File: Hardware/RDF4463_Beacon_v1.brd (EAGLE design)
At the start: 100 x 80 mm, 21 parts, among them IC1 LD117AS33TR, M1 DORJI_DRF4463F, U1 PIC18F24K22

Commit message: PCB yi cizmeye basladim
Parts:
- ANT1: value (none) -> ANT
- C1, C2: value (none) -> 15p
- C3: value (none) -> 10n
- LED1: value (none) -> Y
- LED2: value (none) -> K
- Q1: value (none) -> 20M
- R1, R4: value (none) -> 10K
- R2, R3, R5: value (none) -> 1K
- SV1: value (none) -> ICD
- VIN: value (none) -> INPUT
- moved R3 81.1 mm to (-47.0, 44.5), turned to 0 degrees
- moved C4 76.8 mm to (-39.4, 26.7)
- moved LED2 74.5 mm to (-43.2, 50.8), turned to 0 degrees
- moved R2 73.9 mm to (-41.9, 44.5), turned to 0 degrees
- moved C5 71.0 mm to (-27.9, 26.7)
- moved C18 70.5 mm to (-17.8, 38.1), turned to 0 degrees
- moved LED1 68.2 mm to (-36.8, 50.8), turned to 0 degrees
- moved R1 50.7 mm to (-36.8, 44.5), turned to 0 degrees
- moved M1 46.2 mm to (31.8, 45.7)
- moved R5 44.2 mm to (-15.2, 50.8)
- moved C17 43.1 mm to (-48.3, 26.7)
- moved C1 28.4 mm to (19.4, 37.9), turned to 270 degrees
- moved U1 27.6 mm to (32.2, 42.8)
- moved IC1 24.7 mm to (31.8, 53.9)
- moved C2 22.8 mm to (19.4, 45.6), turned to 90 degrees
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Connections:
- removed net GPIO0: M1.3
- removed net GPIO1: M1.4
- removed net N$10: R2.1, R3.1
- removed net N$5: R1.1
- net +3V3: now also M1.6; no longer M1.5
- net GND: now also R2.1, R3.1
- net MCLR: now also R1.1
- net RB6: now also U1.27
- net SCLK: now also U1.24
- net SDI: now also M1.5; no longer M1.7
- net SDO: now also M1.7; no longer M1.6
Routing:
- net GND: track 0.00 -> 23.4 mm
- net N$3: track 0.00 -> 13.6 mm
- net N$4: track 0.00 -> 13.1 mm
- net RB7: track 0.00 -> 8.21 mm
- net RB6: track 0.00 -> 8.11 mm
- net SDN: track 7.13 -> 0.00 mm
- net SDI: track 5.24 -> 0.00 mm
- net SCLK: track 0.00 -> 4.35 mm
- net VCC: track 0.00 -> 3.97 mm
- net N$2: track 0.00 -> 2.17 mm
- net NSEL: track 6.49 -> 4.61 mm
- net NIRQ: track 6.73 -> 4.87 mm
- net SDO: track 5.65 -> 4.23 mm

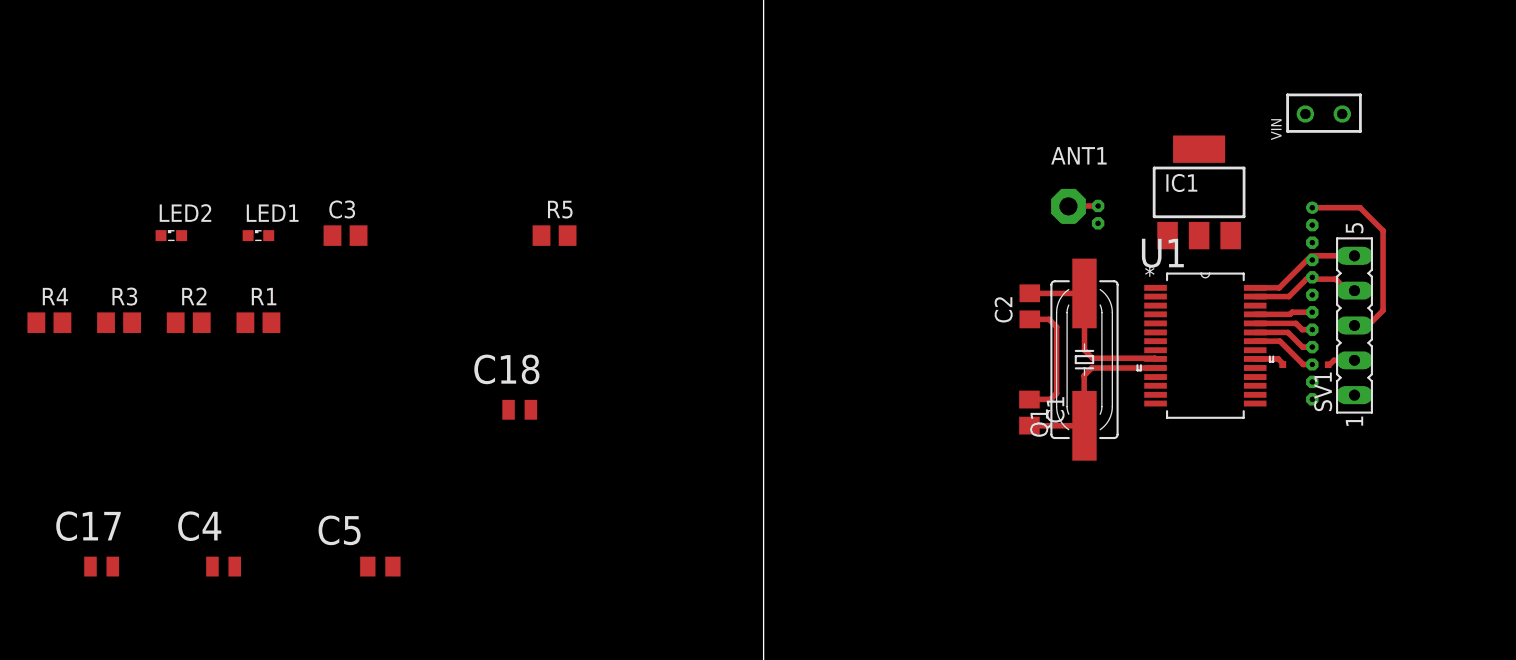
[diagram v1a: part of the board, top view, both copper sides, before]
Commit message: once -SS kilif a gore cizmistim
Bu versiyonda degistiriyorum.. -SO klifli PIC e gorre yaptim

bu kartin buyuk bir bolumunu ICD konnektoru ve DATA RXTX konnektoru tutuyor
simdilik bunu bir EVALUATION karti gibi kullanacagim

Daha sonra yapacaklarim sunlardir :
------------------------------------

1) PIC'i APRS kullanimi icin 16F628 gibi kucuk bir PIC ile degistirmek
2) secilecek PIC'in 3.3V ile calisan versiyonunu tercih etmek
3) MTK GPS i de ekleyip ondan gelen datalari okumak
4) MTK GPS i iceren bir kart cizmek
5) vesaire vesaire
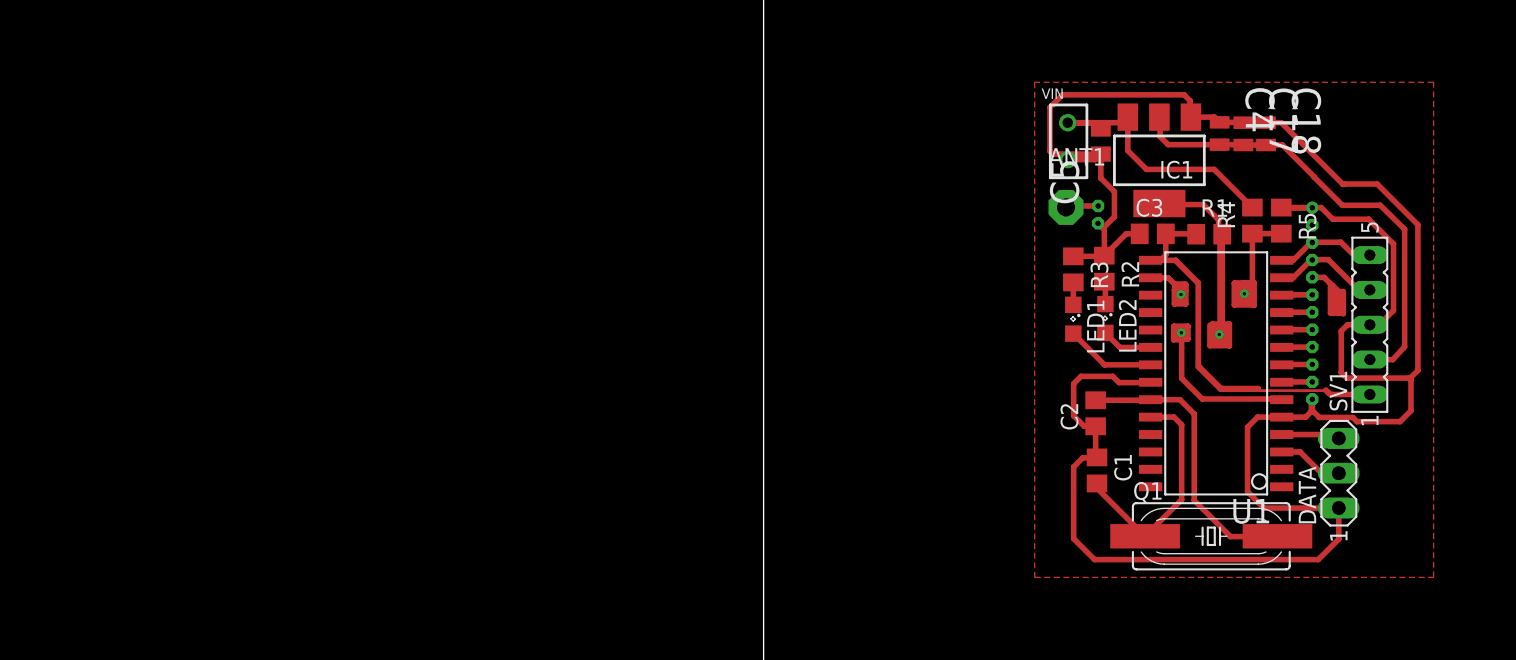
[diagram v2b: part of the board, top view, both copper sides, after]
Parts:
- added DATA: RTX, con-lstb:MA03-1
- LED1, LED2: device led:SML0603 -> led:SML0805
- R5: value 1K -> 1K8
- moved C17 89.0 mm to (35.0, 58.2), turned to 270 degrees
- moved R4 88.0 mm to (35.6, 51.9), turned to 90 degrees
- moved C4 79.2 mm to (33.2, 58.2), turned to 270 degrees
- moved R3 69.7 mm to (22.6, 48.3), turned to 270 degrees
- moved R1 69.6 mm to (32.5, 50.9)
- moved LED2 68.4 mm to (24.9, 44.8), turned to 270 degrees
- moved R2 66.9 mm to (24.8, 48.4), turned to 270 degrees
- moved C5 61.0 mm to (24.6, 57.7), turned to 90 degrees
- moved LED1 59.7 mm to (22.6, 44.7), turned to 270 degrees
- moved C3 58.9 mm to (28.4, 50.9)
- moved C18 58.0 mm to (36.6, 58.2), turned to 270 degrees
- moved R5 53.0 mm to (37.7, 51.9), turned to 270 degrees
- moved VIN 18.1 mm to (22.2, 58.3), turned to 270 degrees
- moved Q1 15.9 mm to (32.6, 28.9), turned to 0 degrees
- moved C2 9.16 mm to (24.2, 37.8)
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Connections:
- removed net +3V3: C17.2, C18.2, C4.2, IC1.4, M1.6
- new net RX: DATA.3, U1.18
- new net TX: DATA.2, U1.17
- net GND: now also DATA.1
- net MCLR: now also C3.2
- net SDI: now also M1.7, U1.25; no longer M1.5, U1.26
- net SDO: now also M1.6, U1.26; no longer M1.7, U1.25
- net VCC: now also C17.2, C18.2, C4.2, IC1.4, M1.5; no longer C3.2
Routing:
- net GND: track 23.4 -> 167.7 mm
- net VCC: track 3.97 -> 67.0 mm
- net MCLR: track 0.00 -> 43.0 mm
- net ADC: track 0.00 -> 28.6 mm
- net VIN: track 0.00 -> 20.4 mm
- net N$11: track 0.00 -> 16.7 mm
- net N$12: track 0.00 -> 11.4 mm
- net N$3: track 13.6 -> 21.2 mm
- net N$6: track 0.00 -> 6.58 mm
- net TX: track 0.00 -> 4.80 mm
- net RX: track 0.00 -> 4.28 mm
- net N$4: track 13.1 -> 17.0 mm
- net N$7: track 0.00 -> 3.74 mm
- net N$10: track 0.00 -> 3.41 mm
- net NIRQ: track 4.87 -> 2.24 mm
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- added copper zone on layer 1, net GND
